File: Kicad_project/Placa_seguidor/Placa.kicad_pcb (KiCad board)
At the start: 2 copper layers, 15 parts, among them J1 Conn_01x02_Female, J2 Conn_01x08_Female, U1 barra2pins, U10 PW_Slinha, U13 Desenho_placa_seguidor, U2 barra3pins, U3 Borne, U4 Borne, U5 Borne, U6 Borne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

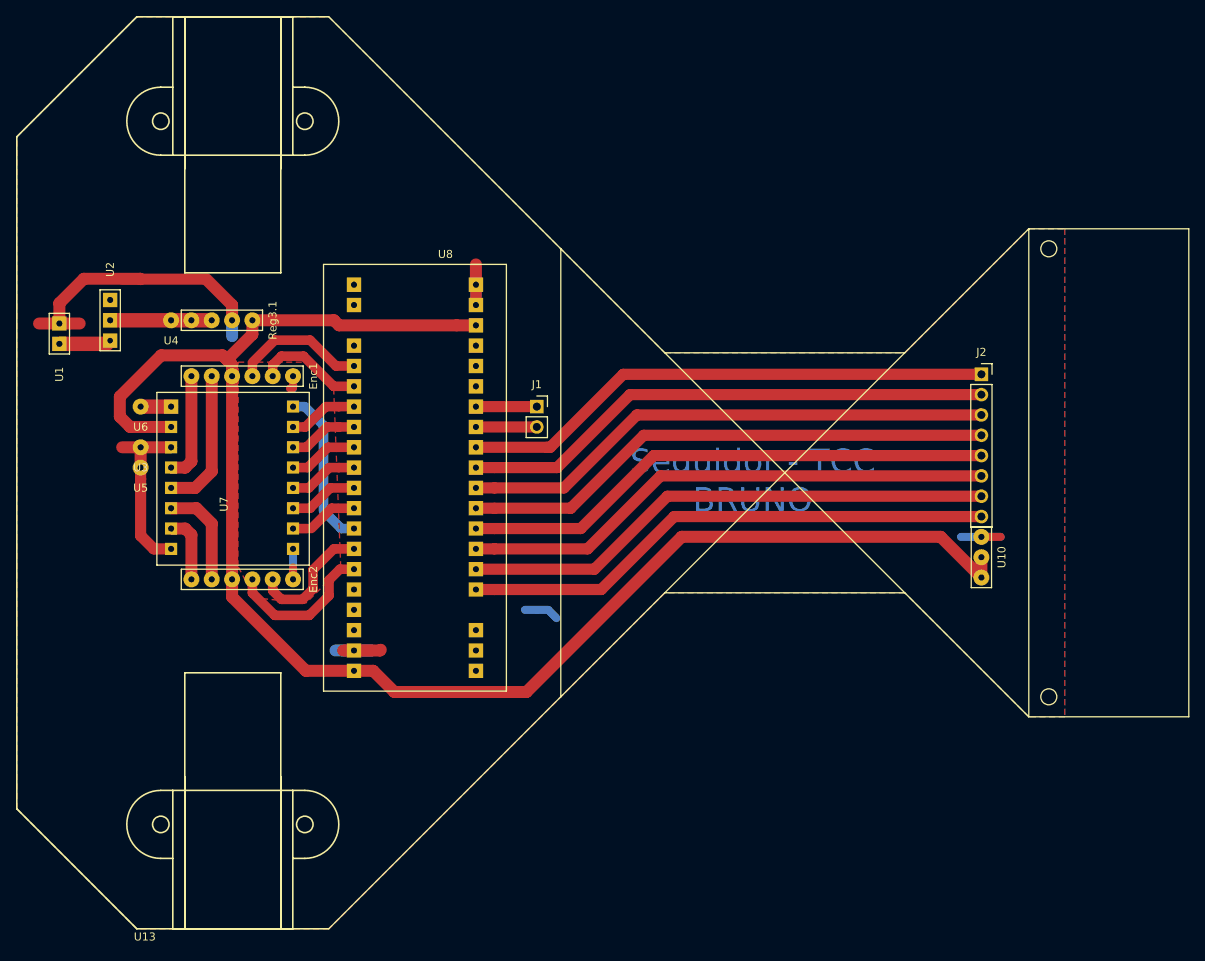
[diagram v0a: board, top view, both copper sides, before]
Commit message: Implemented another control rules
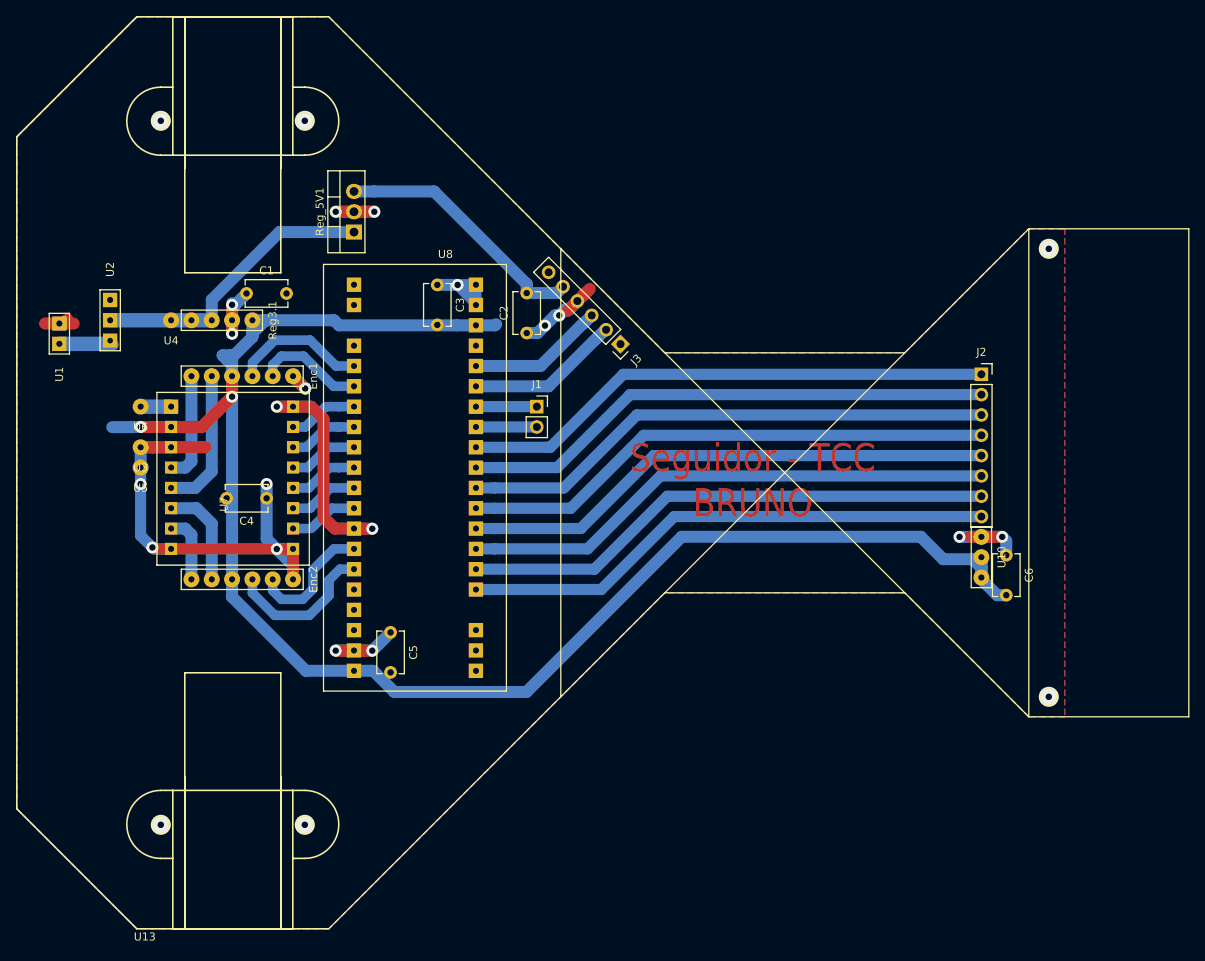
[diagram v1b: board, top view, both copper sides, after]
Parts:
- added C1: C, Capacitor_THT:C_Disc_D5.1mm_W3.2mm_P5.00mm, F.Cu at (43.7, 49.6)
- added C2: C, Capacitor_THT:C_Disc_D5.1mm_W3.2mm_P5.00mm, F.Cu at (78.7, 54.5)
- added C3: C, Capacitor_THT:C_Disc_D5.1mm_W3.2mm_P5.00mm, F.Cu at (67.6, 48.5)
- added C4: C, Capacitor_THT:C_Disc_D5.1mm_W3.2mm_P5.00mm, F.Cu at (46.2, 75.2)
- added C5: C, Capacitor_THT:C_Disc_D5.1mm_W3.2mm_P5.00mm, F.Cu at (61.7, 91.9)
- added C6: C, Capacitor_THT:C_Disc_D5.1mm_W3.2mm_P5.00mm, F.Cu at (138.7, 82.3)
- added J3: Conn_01x06_Female, Connector_PinSocket_2.54mm:PinSocket_1x06_P2.54mm_Vertical, F.Cu at (90.5, 55.9)
- added Reg_5V1: LM7805, Package_TO_SOT_THT:TO-220-3_Vertical, F.Cu at (57.1, 41.9)
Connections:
- U8 pad 35: Net-(U8-Pad35) -> /RX_module
- U8 pad 36: Net-(U8-Pad36) -> /TX_module
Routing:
- net /GND: track 101.1 -> 137.2 mm, vias 0 -> 22
- net /V5: track 0.00 -> 32.4 mm
- net /VCC: track 12.7 -> 36.5 mm
- net /RX_module: track 0.00 -> 19.2 mm
- net /TX_module: track 0.00 -> 17.0 mm
- net /V3.3: track 200.6 -> 212.0 mm, vias 0 -> 2
- net /PWM_E: track 20.2 -> 29.8 mm, vias 0 -> 2
- net /VBat: track 6.52 -> 7.18 mm
- added copper zone on B.Cu, net /V3.3
- removed copper zone on B.Cu, net /GND
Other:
- net class Default: via_dia 0.6 -> 1.5; via_drill 0.4 -> 0.8

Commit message: it seems to be working now
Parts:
- removed C1, C2, C3, C4, C5, C6: C, Capacitor_THT:C_Disc_D5.1mm_W3.2mm_P5.00mm
- added F1: Fuse_Small, Resistor_THT:R_Axial_DIN0309_L9.0mm_D3.2mm_P5.08mm_Vertical, F.Cu at (20.3, 61.0)
- U2: value barra3pins -> barra2pins; footprint FootLibAlan:barra3pins -> FootLibAlan:barra2pins
- moved U3 42.2 mm to (19.3, 109.5)
- moved U5 11.3 mm to (19.6, 68.3)
- moved U2 0.41 mm to (26.7, 53.3)
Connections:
- U2 pad 1: /VBat -> /Vfuse
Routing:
- net /V3.3: track 212.0 -> 190.3 mm, vias 2 -> 0
- net /GND: track 137.2 -> 120.7 mm, vias 22 -> 18
- net /Vfuse: track 0.00 -> 5.61 mm
- net /VBat: track 7.18 -> 5.08 mm
- net /VCC: track 36.5 -> 37.9 mm
- net /V5: track 32.4 -> 31.7 mm
- net (no net): vias 0 -> 6
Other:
- net class Default: trace_width 1.5 -> 1.8
